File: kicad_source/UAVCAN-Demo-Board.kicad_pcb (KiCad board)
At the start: 2 copper layers, 21 x 25 mm, 31 parts, among them CN1 ARDUINO_NANO_33, CN2 691322310004, CN3 GH_SM04B-GHS-TB, CN4 GH_SM04B-GHS-TB, CN5 691322310004, CN6 691322310004, SW1 TAST_VER, U1 MCP2515, U2 SN65VHD232, U3 DS18B20

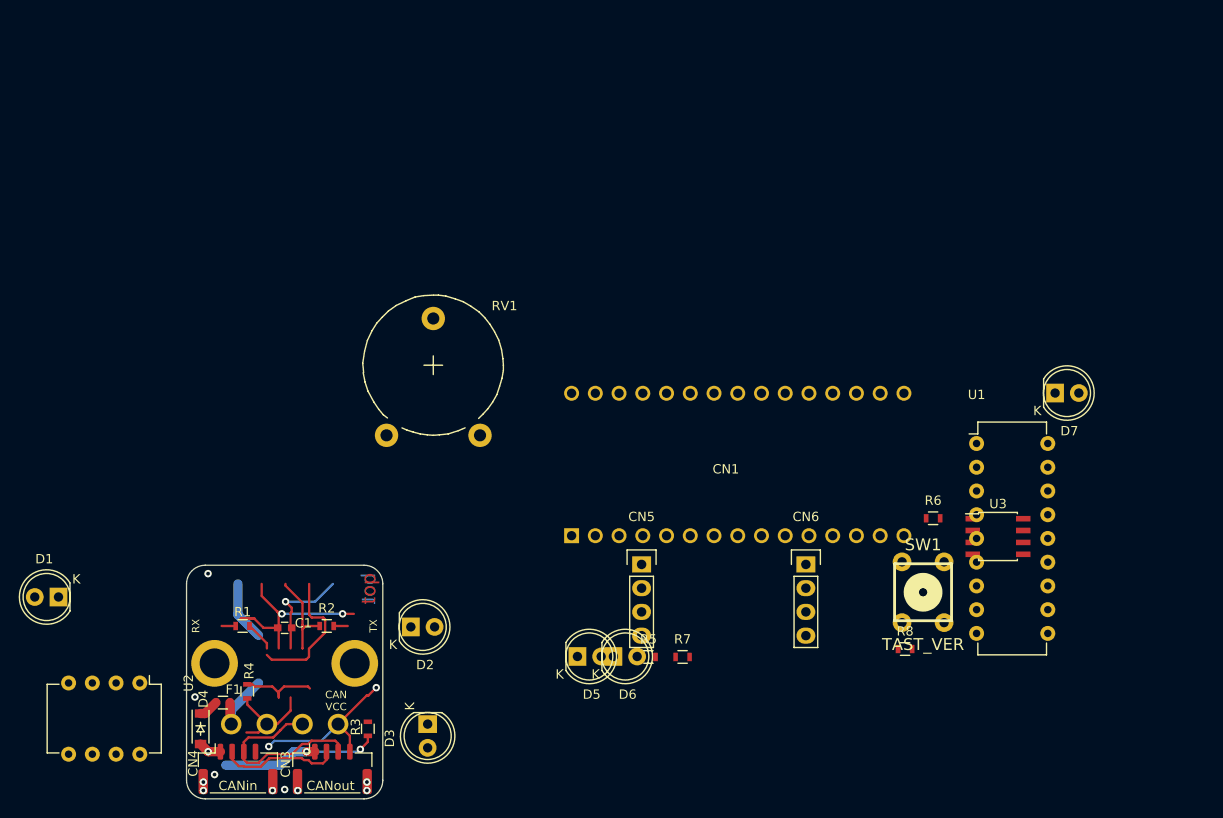
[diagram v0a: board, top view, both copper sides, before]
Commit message: switched to THT parts
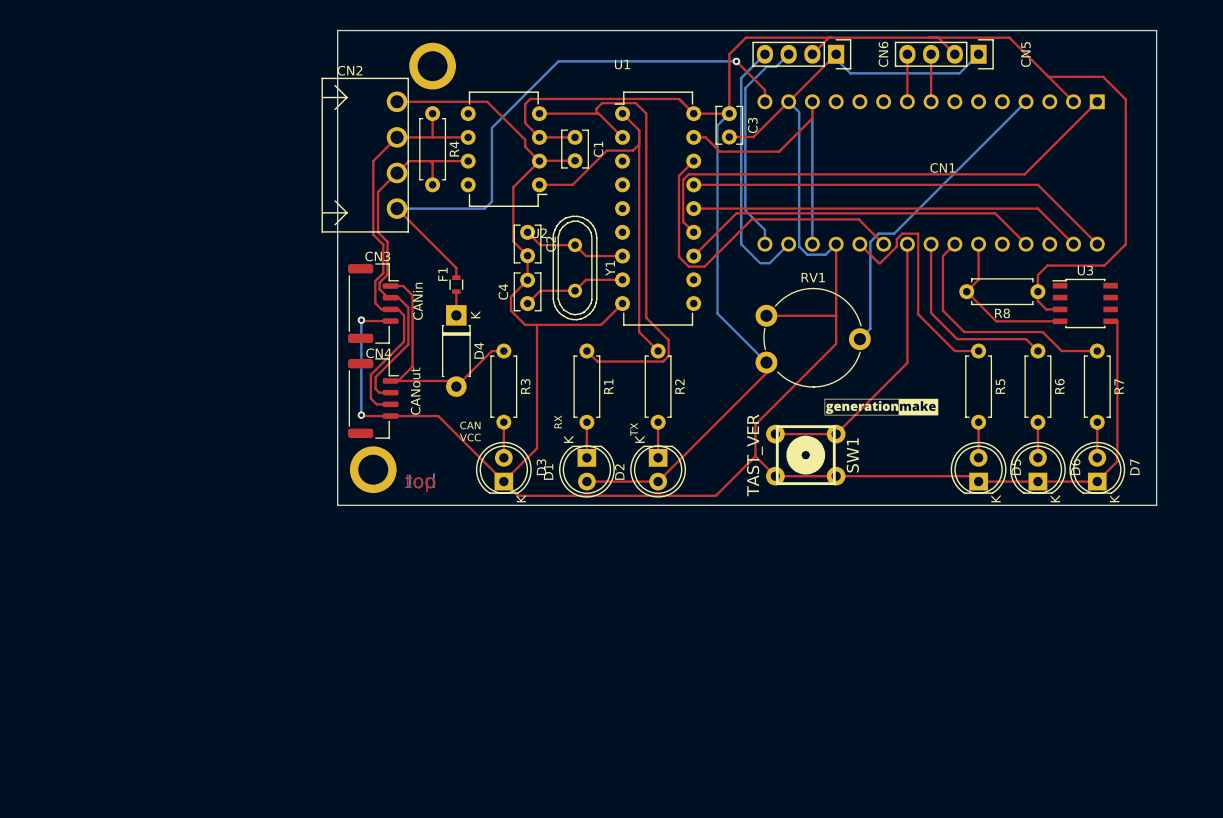
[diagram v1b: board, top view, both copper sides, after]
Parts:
- added C2: 18pF, Capacitor_THT:C_Disc_D3.8mm_W2.6mm_P2.50mm, F.Cu at (174.0, 55.9)
- added C3: 100nF, Capacitor_THT:C_Disc_D3.8mm_W2.6mm_P2.50mm, F.Cu at (195.6, 43.2)
- added C4: 18pF, Capacitor_THT:C_Disc_D3.8mm_W2.6mm_P2.50mm, F.Cu at (174.0, 63.5)
- added Y1: 16 MHz, crystals:Crystal_HC49-U_Vertical, F.Cu at (179.1, 59.7)
- C1: footprint capacitors:C_0603 -> Capacitor_THT:C_Disc_D3.8mm_W2.6mm_P2.50mm
- CN2, L1: moved to F.Cu
- D4: footprint diodes:SOD-123 -> Diode_THT:D_DO-41_SOD81_P7.62mm_Horizontal
- R1, R2, R3, R4, R5, R6, R7, R8: footprint resistors:R_0603 -> Resistor_THT:R_Axial_DIN0207_L6.3mm_D2.5mm_P7.62mm_Horizontal
- RV1: footprint potentiometers:Potentiometer_Trimmer-Piher_PT15-V12-5_horizontal -> Potentiometer_THT:Potentiometer_Piher_PT-10-V10_Vertical
- moved U2 68.3 mm to (175.3, 50.8), turned to 180 degrees
- moved L1 68.1 mm to (211.8, 77.2), turned to 0 degrees
- moved MECH1 68.0 mm to (163.8, 38.1)
- moved CN5 65.4 mm to (222.2, 36.8), turned to 270 degrees
- moved R4 64.9 mm to (163.8, 43.2)
- moved CN2 62.1 mm to (160.0, 47.6), turned to 270 degrees
- moved C1 61.0 mm to (179.1, 45.7), turned to 270 degrees
- moved D1 58.5 mm to (180.3, 80.0), turned to 270 degrees
- moved R7 55.1 mm to (234.9, 68.6), turned to 270 degrees
- moved CN6 54.7 mm to (207.0, 36.8), turned to 270 degrees
- moved D4 52.0 mm to (166.4, 64.8)
- moved U1 51.8 mm to (184.2, 43.2)
- moved F1 51.2 mm to (166.4, 61.5), turned to 270 degrees
- moved CN3 50.0 mm to (157.5, 63.5), turned to 270 degrees
- moved D6 49.1 mm to (228.6, 82.5), turned to 90 degrees
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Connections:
- U1 pad 7: (no net) -> Net-(C2-Pad1)
- U1 pad 8: (no net) -> Net-(C4-Pad1)
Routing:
- net GND: track 28.9 -> 276.5 mm, vias 7 -> 2
- net +3V3: track 22.0 -> 179.9 mm, vias 2 -> 0
- net /SPI_SCK: track 0.00 -> 53.8 mm
- net +5V: track 14.4 -> 63.1 mm, vias 0 -> 1
- net /SPI_MISO: track 0.00 -> 45.8 mm
- net /SPI_MOSI: track 0.00 -> 42.2 mm
- net /MCP2515_INT: track 0.00 -> 38.8 mm
- net /MCP2515_CS: track 0.00 -> 36.4 mm
- net /CAN_RX: track 18.2 -> 52.9 mm
- net /ANALOG: track 0.00 -> 33.7 mm
- net /RESET: track 0.00 -> 31.8 mm
- net /CAN_TX: track 10.1 -> 41.0 mm
- net /SWITCH: track 0.00 -> 30.0 mm
- net /SERIAL_RX: track 0.00 -> 28.1 mm
- net /LED3: track 0.00 -> 25.9 mm
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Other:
- board size 21 x 25 mm -> 87.6 x 50.8 mm
- board text removed: "3V3"
- board text removed: "5V"
- board text removed: "CAN RX"
- board text removed: "CAN TX"
- board text removed: "Dronecode CANAdapter 0.2"

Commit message: changed DS18B20 to TO-92, cleaned up layout, added labels
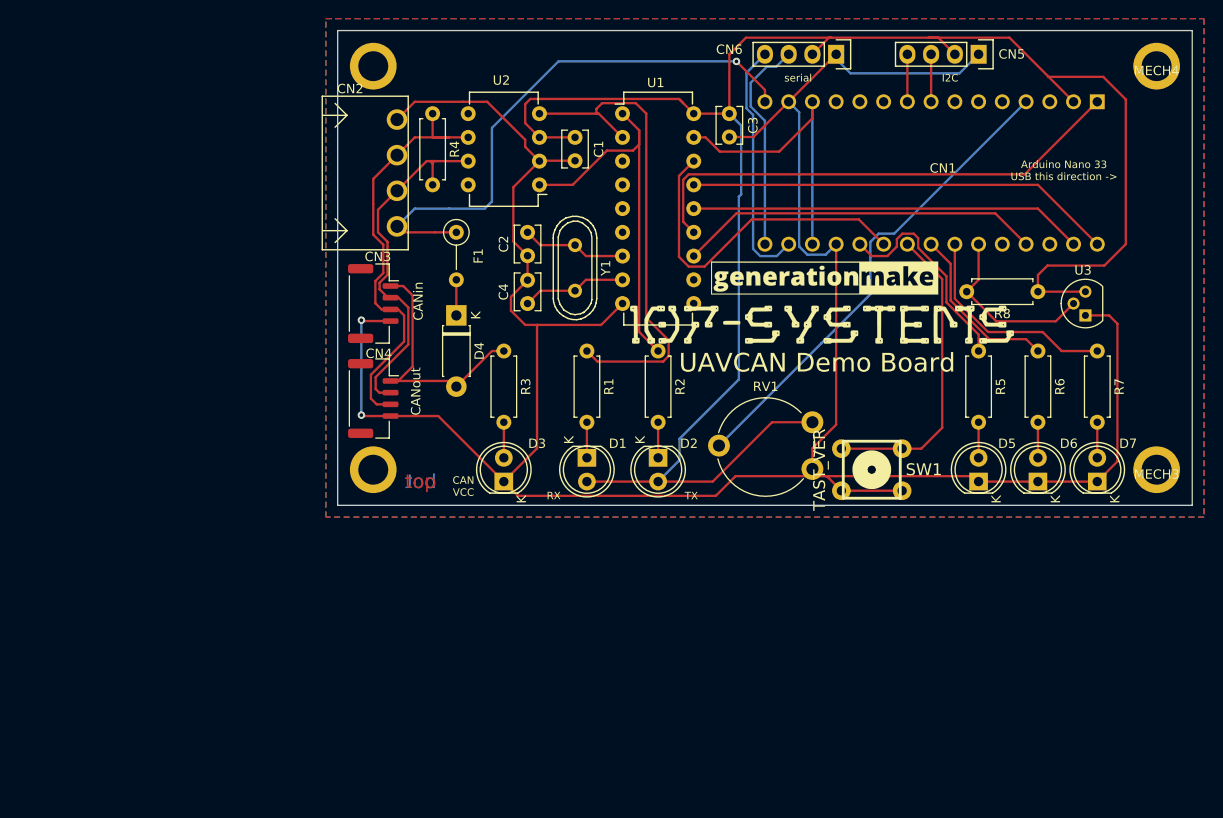
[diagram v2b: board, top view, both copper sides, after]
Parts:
- added L2: Label, labels:107-systems_logo, F.Cu at (205.5, 65.8)
- added MECH3: MHP_3.2_5.0, MECH_mounting_holes:MHP_3.2_5.0, F.Cu at (241.3, 81.3)
- added MECH4: MHP_3.2_5.0, MECH_mounting_holes:MHP_3.2_5.0, F.Cu at (241.3, 38.1)
- F1: footprint resistors:R_0603 -> Resistor_THT:R_Axial_DIN0207_L6.3mm_D2.5mm_P5.08mm_Vertical
- L1: footprint labels:generationmake_small_silk -> labels:generationmake_logo
- U3: footprint SOIC:SOIC-8_3.9x4.9mm_Pitch1.27mm -> Package_TO_SOT_THT:TO-92
- moved L1 12.7 mm to (205.7, 66.0)
- moved RV1 8.06 mm to (204.5, 76.2), turned to 180 degrees
- moved SW1 7.23 mm to (210.8, 81.3)
- moved MECH1 6.35 mm to (157.5, 38.1)
- moved F1 5.60 mm to (166.4, 55.9)
- moved CN2 1.91 mm to (160.0, 49.5)
- moved U3 1.27 mm to (233.7, 64.8), turned to 90 degrees
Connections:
- U3 pad 1: (no net) -> GND
- U3 pad 2: (no net) -> /ONEWIRE
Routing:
- net /ANALOG: track 33.7 -> 51.4 mm
- net +3V3: track 179.9 -> 197.0 mm
- net /SWITCH: track 30.0 -> 32.9 mm
- net +5V: track 63.1 -> 60.4 mm
- net /LED3: track 25.9 -> 23.4 mm
- net /LED1: track 25.6 -> 23.2 mm
- net /ONEWIRE: track 16.9 -> 19.1 mm
- net /LED2: track 20.5 -> 18.5 mm
- net GND: track 276.5 -> 278.5 mm
- net /SERIAL_RX: track 28.1 -> 26.6 mm
- net /CANVCC_F: track 2.54 -> 3.81 mm
- net /CANL: track 46.1 -> 46.8 mm
- net /CANH: track 40.7 -> 40.1 mm
- added copper zone on B.Cu, net GND
- added copper zone on F.Cu, net GND
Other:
- board size 87.6 x 50.8 mm -> 91.4 x 50.8 mm
- board text added: "Arduino Nano 33 USB this direction ->"
- board text added: "I2C"
- board text added: "UAVCAN Demo Board"
- board text added: "serial"
